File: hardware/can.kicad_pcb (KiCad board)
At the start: 2 copper layers, 45 x 35 mm, 39 parts, among them J1 AKL_5_2, J2 AKL_5_2, J3 DB9, P1 CON-SENSOR, SW1 Termination, U1 M24C64, U2 MCP2515, U3 MCP2562, U4 DRILL, U5 DRILL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

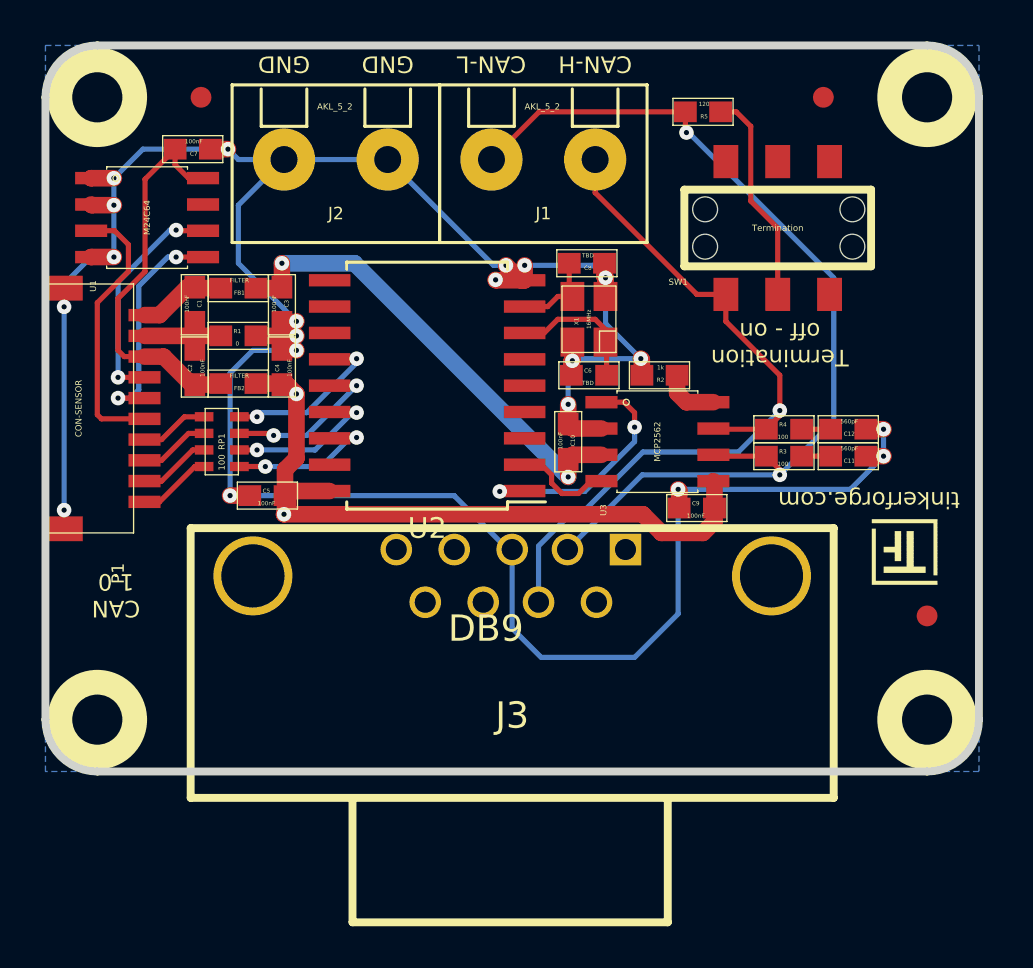
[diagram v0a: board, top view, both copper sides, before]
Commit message: remove serial connector
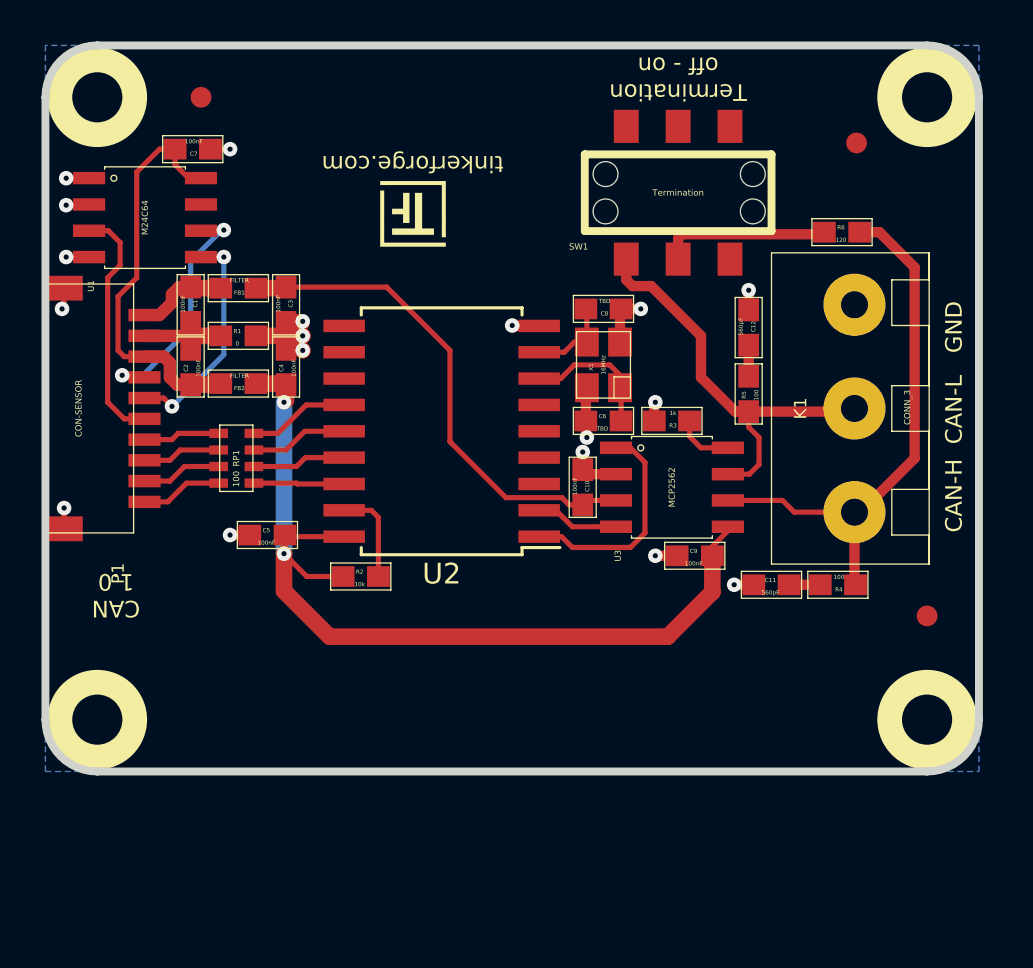
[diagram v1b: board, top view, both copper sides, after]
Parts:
- removed J1, J2: AKL_5_2, kicad-libraries:AKL_5_2
- removed J3: DB9, kicad-libraries:SUB09-EU
- added K1: CONN_3, AKL_5_3, F.Cu at (164.3, 100.6)
- added R6: 120, kicad-libraries:0603E, F.Cu at (163.7, 92.1)
- R2: value 1k -> 10k
- R3: value 100 -> 1k
- R5: value 120 -> 100
- moved G*** 28.8 mm to (144.6, 92.8)
- moved R2 17.4 mm to (140.5, 108.7), turned to 180 degrees
- moved R5 13.8 mm to (159.2, 99.9), turned to 270 degrees
- moved R4 7.94 mm to (163.5, 109.1), turned to 0 degrees
- moved C11 7.22 mm to (160.3, 109.1), turned to 180 degrees
- moved C12 6.86 mm to (159.2, 96.7), turned to 90 degrees
- moved R3 5.66 mm to (155.5, 101.2), turned to 0 degrees
- moved SW1 5.09 mm to (155.8, 90.2)
- moved Fiducial_Mark 2.72 mm to (164.4, 87.8)
- moved C8 2.34 mm to (152.2, 95.8)
- moved U2 2.31 mm to (144.4, 101.7)
- moved C10 2.31 mm to (151.2, 104.4)
- moved C6 2.31 mm to (152.2, 101.2)
- moved U3 2.31 mm to (155.5, 104.4)
- moved VAL 2.31 mm to (144.0, 102.8)
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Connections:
- R2 pad 1: GND -> Net-(R2-Pad1)
- R2 pad 2: Net-(R2-Pad2) -> VCC
- R3 pad 1: Net-(C11-Pad1) -> GND
- R3 pad 2: Net-(J1-Pad1) -> Net-(R3-Pad2)
- R4 pad 1: Net-(C12-Pad1) -> Net-(C11-Pad1)
- R4 pad 2: Net-(J1-Pad2) -> Net-(K1-Pad3)
- R5 pad 1: Net-(J1-Pad1) -> Net-(C12-Pad1)
- R5 pad 2: Net-(R5-Pad2) -> Net-(K1-Pad2)
- SW1 pad 1: Net-(J1-Pad2) -> Net-(K1-Pad2)
- SW1 pad 2: Net-(R5-Pad2) -> Net-(R6-Pad2)
- U2 pad 17: (no net) -> Net-(R2-Pad1)
- U3 pad 6: Net-(J1-Pad1) -> Net-(K1-Pad3)
- U3 pad 7: Net-(J1-Pad2) -> Net-(K1-Pad2)
- U3 pad 8: Net-(R2-Pad2) -> Net-(R3-Pad2)
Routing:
- net GND: track 143.4 -> 25.5 mm, vias 20 -> 18
- net Net-(J1-Pad1): track 47.4 -> 0.00 mm, vias 2 -> 0
- net Net-(J1-Pad2): track 37.4 -> 0.00 mm, vias 1 -> 0
- net Net-(K1-Pad3): track 0.00 -> 26.4 mm
- net Net-(K1-Pad2): track 0.00 -> 20.3 mm
- net VCC: track 33.8 -> 44.5 mm
- net Net-(R5-Pad2): track 10.4 -> 0.00 mm
- net Net-(R6-Pad2): track 0.00 -> 8.17 mm
- net Net-(R2-Pad1): track 0.00 -> 4.64 mm
- net Net-(RP1-Pad4): track 8.44 -> 4.92 mm, vias 2 -> 0
- net Net-(RP1-Pad3): track 7.98 -> 4.72 mm, vias 2 -> 0
- net Net-(RP1-Pad2): track 7.71 -> 4.53 mm, vias 2 -> 0
- net Net-(RP1-Pad1): track 7.55 -> 4.37 mm, vias 2 -> 0
- net Net-(R3-Pad2): track 0.00 -> 2.82 mm
- net Net-(R2-Pad2): track 2.78 -> 0.00 mm
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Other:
- board text added: "CAN-H CAN-L GND"
- board text removed: "CAN-H"
- board text removed: "CAN-L"
- board text removed: "GND"

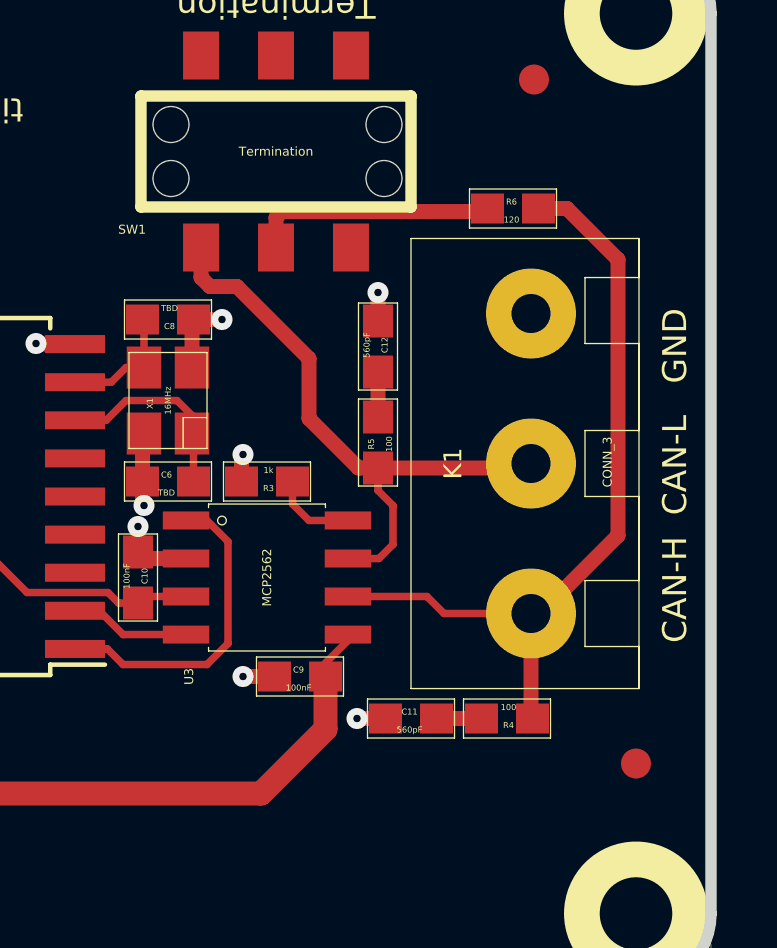
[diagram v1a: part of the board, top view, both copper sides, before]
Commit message: more space between resistors and terminal
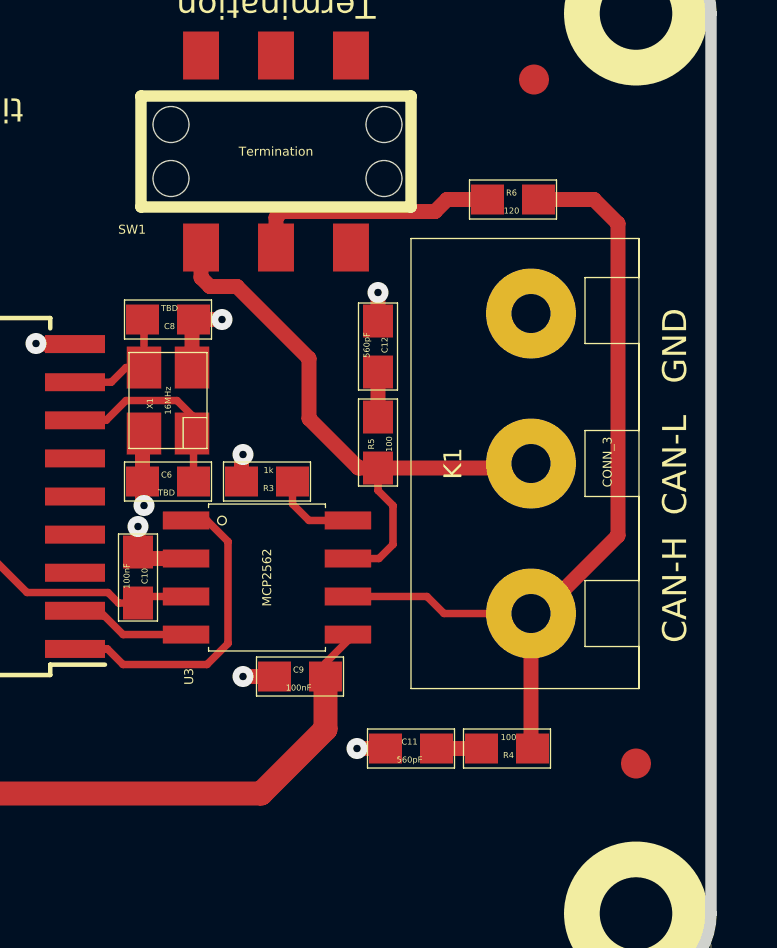
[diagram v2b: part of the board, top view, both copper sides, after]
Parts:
- moved C11 1.00 mm to (160.3, 110.1)
- moved R4 1.00 mm to (163.5, 110.1)
- moved R6 0.30 mm to (163.7, 91.8)
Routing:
- net Net-(K1-Pad3): track 26.4 -> 27.2 mm
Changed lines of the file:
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@@
     (links 67)
     (no_connects 0)
-    (area 125.109499 82.909499 170.490501 118.290501)
+    (area 124.445139 82.245139 282.895869 162.490743)
     (thickness 1.6002)
     (drawings 13)
-    (tracks 224)
+    (tracks 225)
     (zones 0)
     (modules 38)
@@
   (layers
     (0 Vorderseite signal)
-    (31 Rückseite signal)
+    (31 Rückseite signal hide)
     (32 B.Adhes user)
     (33 F.Adhes user)
@@
   )
   (setup
-    (last_trace_width 0.25)
+    (last_trace_width 0.5)
     (user_trace_width 0.25)
     (user_trace_width 0.29972)
@@
     (pad_to_mask_clearance 0)
     (aux_axis_origin 125.30074 118.09984)
-    (visible_elements FFFFFF9F)
+    (visible_elements FFFFFFBF)
     (pcbplotparams
       (layerselection 0x00030_80000001)
@@
   )
   (module kicad-libraries:0603E (layer Vorderseite)
-    (at 160.3 109.1 180)
+    (at 160.3 110.1 180)
     (attr smd)
     (fp_text reference C11 (at 0.05 0.225 180) (layer F.SilkS)
@@
   )
   (module kicad-libraries:0603E (layer Vorderseite)
-    (at 163.5 109.1)
+    (at 163.5 110.1)
     (attr smd)
     (fp_text reference R4 (at 0.05 0.225) (layer F.SilkS)
@@
   )
   (module kicad-libraries:0603E (layer Vorderseite)
-    (at 163.7 92.1 180)
+    (at 163.7 91.8 180)
     (attr smd)
     (fp_text reference R6 (at 0.05 0.225 180) (layer F.SilkS)
@@
   (segment (start 159.2 95.8499) (end 159.2 94.9) (width 0.5) (layer Vorderseite) (net 1))
   (via (at 159.2 94.9) (size 0.70104) (drill 0.24892) (layers Vorderseite Rückseite) (net 1))
-  (segment (start 159.4499 109.1) (end 158.5 109.1) (width 0.5) (layer Vorderseite) (net 1))
-  (via (at 158.5 109.1) (size 0.70104) (drill 0.24892) (layers Vorderseite Rückseite) (net 1))
+  (segment (start 159.4499 110.1) (end 158.5 110.1) (width 0.5) (layer Vorderseite) (net 1))
+  (via (at 158.5 110.1) (size 0.70104) (drill 0.24892) (layers Vorderseite Rückseite) (net 1))
   (segment (start 155.7499 107.7) (end 154.7 107.7) (width 0.5) (layer Vorderseite) (net 1))
   (via (at 154.7 107.7) (size 0.70104) (drill 0.24892) (layers Vorderseite Rückseite) (net 1))
@@
   (segment (start 153.0501 101.2) (end 153.0501 99.64982) (width 0.249) (layer Vorderseite) (net 14))
   (segment (start 153.0501 99.64982) (end 153.0001 99.59982) (width 0.249) (layer Vorderseite) (net 14))
-  (segment (start 162.6499 109.1) (end 161.1501 109.1) (width 0.5) (layer Vorderseite) (net 15))
+  (segment (start 162.6499 110.1) (end 161.1501 110.1) (width 0.5) (layer Vorderseite) (net 15))
   (segment (start 159.2 97.5501) (end 159.2 99.0499) (width 0.5) (layer Vorderseite) (net 16))
   (segment (start 149.1 106.78) (end 150.18 106.78) (width 0.25) (layer Vorderseite) (net 17))
@@
   (segment (start 156.3501 101.9501) (end 156.3501 101.2) (width 0.249) (layer Vorderseite) (net 26))
   (segment (start 156.89754 102.49754) (end 156.3501 101.9501) (width 0.249) (layer Vorderseite) (net 26))
+  (segment (start 162.8499 91.8) (end 161.5 91.8) (width 0.5) (layer Vorderseite) (net 27))
+  (segment (start 161.5 91.8) (end 161.1 92.2) (width 0.5) (layer Vorderseite) (net 27))
   (segment (start 155.8 93.4004) (end 155.8 92.4) (width 0.5) (layer Vorderseite) (net 27))
-  (segment (start 156 92.2) (end 162.7499 92.2) (width 0.5) (layer Vorderseite) (net 27))
+  (segment (start 156 92.2) (end 161.1 92.2) (width 0.5) (layer Vorderseite) (net 27))
   (segment (start 155.8 92.4) (end 156 92.2) (width 0.5) (layer Vorderseite) (net 27))
-  (segment (start 162.7499 92.2) (end 162.8499 92.1) (width 0.5) (layer Vorderseite) (net 27))
+  (segment (start 164.5501 91.8) (end 166.4 91.8) (width 0.5) (layer Vorderseite) (net 28))
+  (segment (start 167.2 92.6) (end 167.2 103) (width 0.5) (layer Vorderseite) (net 28))
+  (segment (start 166.4 91.8) (end 167.2 92.6) (width 0.5) (layer Vorderseite) (net 28))
   (segment (start 164.3 105.6) (end 164.6 105.6) (width 0.5) (layer Vorderseite) (net 28))
   (segment (start 164.6 105.6) (end 167.2 103) (width 0.5) (layer Vorderseite) (net 28))
-  (segment (start 165.5 92.1) (end 164.5501 92.1) (width 0.5) (layer Vorderseite) (net 28))
-  (segment (start 167.2 93.8) (end 165.5 92.1) (width 0.5) (layer Vorderseite) (net 28))
-  (segment (start 167.2 103) (end 167.2 93.8) (width 0.5) (layer Vorderseite) (net 28))
   (segment (start 158.19748 105.03246) (end 160.83246 105.03246) (width 0.249) (layer Vorderseite) (net 28))
   (segment (start 161.4 105.6) (end 164.3 105.6) (width 0.249) (layer Vorderseite) (net 28))
   (segment (start 160.83246 105.03246) (end 161.4 105.6) (width 0.249) (layer Vorderseite) (net 28))
-  (segment (start 164.3 105.6) (end 164.3 109.0499) (width 0.5) (layer Vorderseite) (net 28))
-  (segment (start 164.3 109.0499) (end 164.3501 109.1) (width 0.249) (layer Vorderseite) (net 28))
+  (segment (start 164.3 106.6) (end 164.3 110.0499) (width 0.5) (layer Vorderseite) (net 28))
+  (segment (start 164.3 110.0499) (end 164.3501 110.1) (width 0.249) (layer Vorderseite) (net 28))
   (zone (net 1) (net_name GND) (layer Rückseite) (hatch edge 0.508)
     (connect_pads (clearance 0.15))

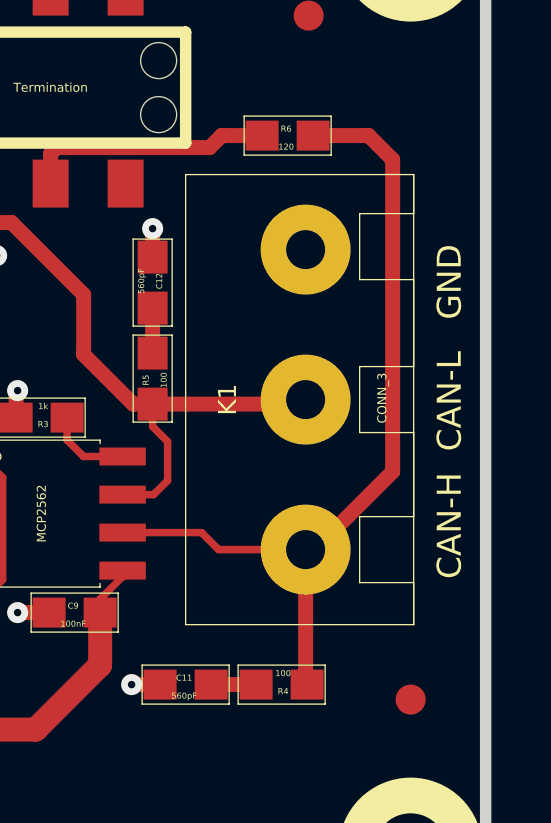
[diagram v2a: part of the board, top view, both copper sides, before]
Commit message: fix can-h/can-l labeling
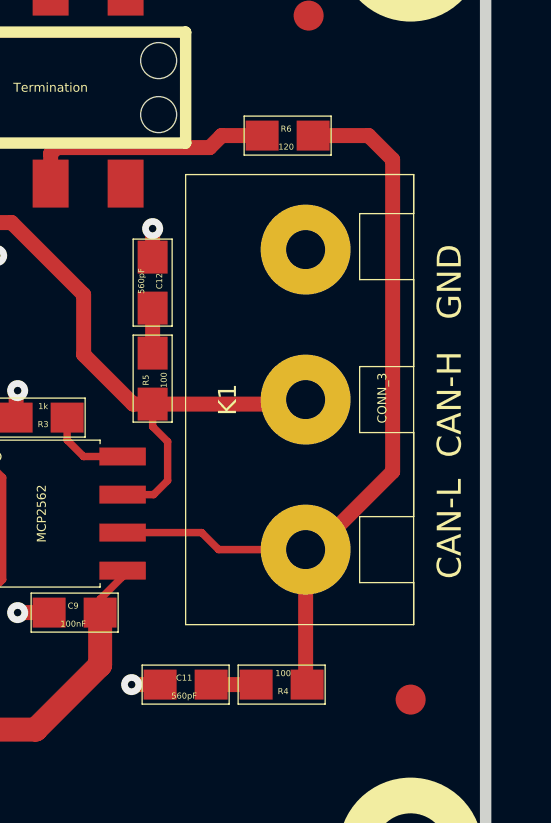
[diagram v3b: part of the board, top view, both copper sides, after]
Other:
- board text added: "CAN-L CAN-H GND"
- board text removed: "CAN-H CAN-L GND"
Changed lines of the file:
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@@
   )
   (setup
-    (last_trace_width 0.5)
+    (last_trace_width 0.249)
     (user_trace_width 0.25)
     (user_trace_width 0.29972)
@@
     (effects (font (size 0.8 0.8) (thickness 0.15)))
   )
-  (gr_text "CAN-H  CAN-L   GND" (at 169.1 101 90) (layer F.SilkS)
+  (gr_text "CAN-L  CAN-H   GND" (at 169.1 101 90) (layer F.SilkS)
     (effects (font (size 0.8 0.8) (thickness 0.15)))
   )

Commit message: adapt filter values
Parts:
- C11, C12: value 560pF -> 470pF
- C6, C8: value TBD -> DNP
- R4, R5: value 100 -> 120
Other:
- board text added: "Copyright Tinkerforge GmbH 2016. This documentation describes Open Hardware and is licensed under the CERN OHL v. 1.1. You may redistribute and modify this documentation under the terms of the CERN OHL v.1.1. (http://ohwr.org/cernohl). This documentation is distributed WITHOUT ANY EXPRESS OR IMPLIED WARRANTY, INCLUDING OF MERCHANTABILITY, SATISFACTORY QUALITY AND FITNESS FOR A PARTICULAR PURPOSE.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"
- board text removed: "Copyright Tinkerforge GmbH 2015. This documentation describes Open Hardware and is licensed under the CERN OHL v. 1.1. You may redistribute and modify this documentation under the terms of the CERN OHL v.1.1. (http://ohwr.org/cernohl). This documentation is distributed WITHOUT ANY EXPRESS OR IMPLIED WARRANTY, INCLUDING OF MERCHANTABILITY, SATISFACTORY QUALITY AND FITNESS FOR A PARTICULAR PURPOSE.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"
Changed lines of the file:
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@@
   (module kicad-libraries:CON-SENSOR (layer Vorderseite)
     (at 125.3 100.6 270)
-    (fp_text reference P1 (at 7.9502 -3.50012 270) (layer F.SilkS)
+    (fp_text reference P1 (at 4.7 -2.9 270) (layer F.SilkS)
       (effects (font (size 0.59944 0.59944) (thickness 0.12446)))
     )
@@
       (effects (font (size 0.2 0.2) (thickness 0.05)))
     )
-    (fp_text value TBD (at 0.05 -0.375 180) (layer F.SilkS)
+    (fp_text value DNP (at 0.05 -0.375 180) (layer F.SilkS)
       (effects (font (size 0.2 0.2) (thickness 0.05)))
     )
@@
       (effects (font (size 0.2 0.2) (thickness 0.05)))
     )
-    (fp_text value TBD (at 0.05 -0.375) (layer F.SilkS)
+    (fp_text value DNP (at 0.05 -0.375) (layer F.SilkS)
       (effects (font (size 0.2 0.2) (thickness 0.05)))
     )
@@
       (effects (font (size 0.2 0.2) (thickness 0.05)))
     )
-    (fp_text value 560pF (at 0.05 -0.375 180) (layer F.SilkS)
+    (fp_text value 470pF (at 0.05 -0.375 180) (layer F.SilkS)
       (effects (font (size 0.2 0.2) (thickness 0.05)))
     )
@@
       (effects (font (size 0.2 0.2) (thickness 0.05)))
     )
-    (fp_text value 560pF (at 0.05 -0.375 90) (layer F.SilkS)
+    (fp_text value 470pF (at 0.05 -0.375 90) (layer F.SilkS)
       (effects (font (size 0.2 0.2) (thickness 0.05)))
     )
@@
       (effects (font (size 0.2 0.2) (thickness 0.05)))
     )
-    (fp_text value 100 (at 0.05 -0.375) (layer F.SilkS)
+    (fp_text value 120 (at 0.05 -0.375) (layer F.SilkS)
       (effects (font (size 0.2 0.2) (thickness 0.05)))
     )
@@
       (effects (font (size 0.2 0.2) (thickness 0.05)))
     )
-    (fp_text value 100 (at 0.05 -0.375 270) (layer F.SilkS)
+    (fp_text value 120 (at 0.05 -0.375 270) (layer F.SilkS)
       (effects (font (size 0.2 0.2) (thickness 0.05)))
     )
@@
   (gr_arc (start 127.8 85.6) (end 125.3 85.6) (angle 90) (layer Edge.Cuts) (width 0.381))
   (gr_arc (start 127.8 115.6) (end 127.8 118.1) (angle 90) (layer Edge.Cuts) (width 0.381))
-  (gr_text "Copyright Tinkerforge GmbH 2015.\nThis documentation describes Open Hardware and is licensed under the\nCERN OHL v. 1.1.\nYou may redistribute and modify this documentation under the terms of the\nCERN OHL v.1.1. (http://ohwr.org/cernohl). This documentation is distributed\nWITHOUT ANY EXPRESS OR IMPLIED WARRANTY, INCLUDING OF\nMERCHANTABILITY, SATISFACTORY QUALITY AND FITNESS FOR A\nPARTICULAR PURPOSE. Please see the CERN OHL v.1.1 for applicable\nconditions" (at 258.8 156.55) (layer Cmts.User)
+  (gr_text "Copyright Tinkerforge GmbH 2016.\nThis documentation describes Open Hardware and is licensed under the\nCERN OHL v. 1.1.\nYou may redistribute and modify this documentation under the terms of the\nCERN OHL v.1.1. (http://ohwr.org/cernohl). This documentation is distributed\nWITHOUT ANY EXPRESS OR IMPLIED WARRANTY, INCLUDING OF\nMERCHANTABILITY, SATISFACTORY QUALITY AND FITNESS FOR A\nPARTICULAR PURPOSE. Please see the CERN OHL v.1.1 for applicable\nconditions" (at 258.8 156.55) (layer Cmts.User)
     (effects (font (size 0.8001 0.8001) (thickness 0.200025) italic))
   )

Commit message: Add 3d information (final)
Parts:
- C1, C10, C11, C12, C2, C3, C4, C5, C6, C7, C8, C9, FB1, FB2: footprint kicad-libraries:0603E -> kicad-libraries:C0603E
- Fiducial_Mark (x3): footprint Fiducial_Mark -> kicad-libraries:Fiducial_Mark
- G***: footprint Logo_31x31 -> kicad-libraries:Logo_31x31
- K1: footprint AKL_5_3 -> kicad-libraries:AKL_5_3
- R1, R2, R3, R4, R5, R6: footprint kicad-libraries:0603E -> kicad-libraries:R0603E
- VAL: footprint WEEE_7mm -> kicad-libraries:WEEE_7mm
- VAL: footprint CE_5mm -> kicad-libraries:CE_5mm
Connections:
- U1 pad 7: (no net) -> Net-(U1-Pad7)
- U2 pad 10: (no net) -> Net-(U2-Pad10)
- U2 pad 11: (no net) -> Net-(U2-Pad11)
- U2 pad 12: (no net) -> Net-(U2-Pad12)
- U2 pad 3: (no net) -> Net-(U2-Pad3)
- U2 pad 4: (no net) -> Net-(U2-Pad4)
- U2 pad 5: (no net) -> Net-(U2-Pad5)
- U2 pad 6: (no net) -> Net-(U2-Pad6)
